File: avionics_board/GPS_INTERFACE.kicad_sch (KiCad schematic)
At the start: 2 parts, among them J6 Conn_01x05

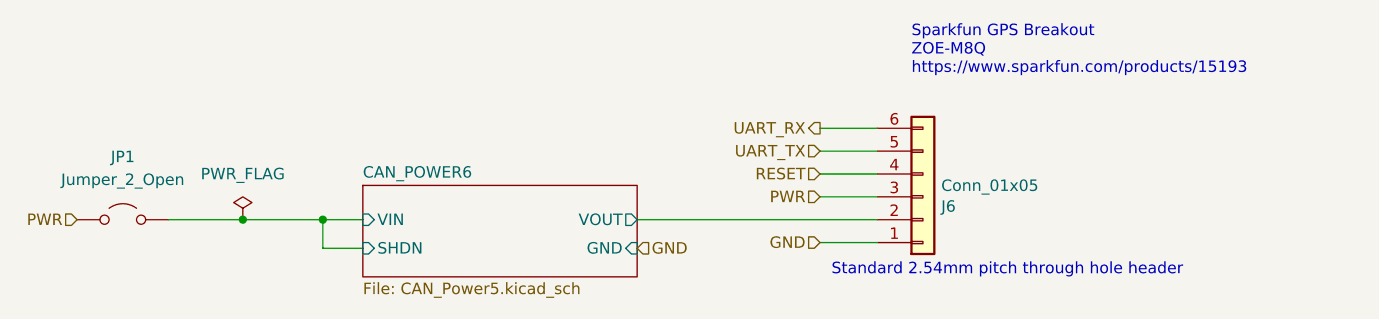
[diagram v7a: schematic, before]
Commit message: refactor AVI into nicer hierarchical components
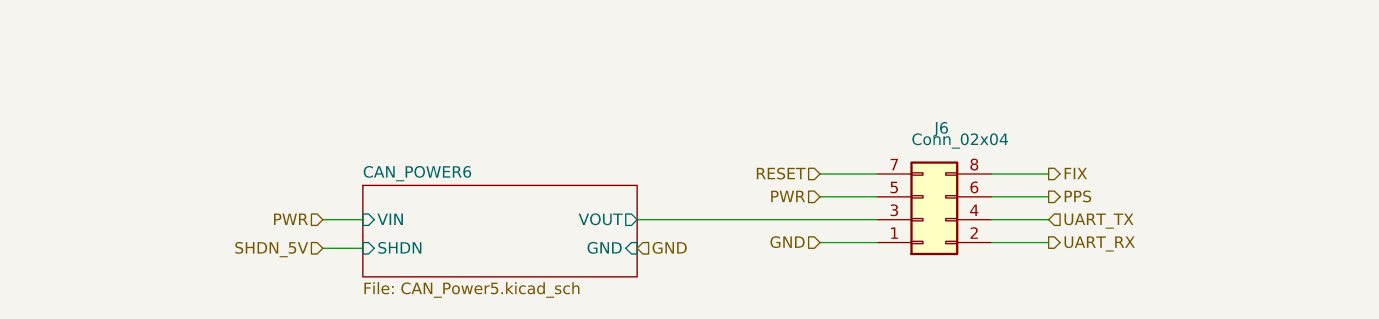
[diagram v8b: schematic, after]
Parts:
- removed J6: Conn_01x05, Connector_PinHeader_2.54mm:PinHeader_1x06_P2.54mm_Vertical, symbol Connector_Generic:Conn_01x06
- removed JP1: Jumper_2_Open, Connector_PinHeader_2.54mm:PinHeader_1x02_P2.54mm_Vertical, symbol Jumper:Jumper_2_Open
- added J6: Conn_02x04, Connector_PinHeader_2.54mm:PinHeader_2x04_P2.54mm_Vertical, symbol Connector_Generic:Conn_02x04_Odd_Even
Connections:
- net CAN_POWER6/VOUT: now also J6.3 (Pin_3)
- net GND: now also J6.1 (Pin_1)
- net PWR: now also J6.5 (Pin_5)
- net RESET: now also J6.7 (Pin_7)
- net UART_RX: now also J6.2 (Pin_2)
- net UART_TX: now also J6.4 (Pin_4)
- new net FIX: J6.8 (Pin_8)
- new net PPS: J6.6 (Pin_6)
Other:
- note removed: "Sparkfun GPS Breakout ZOE-M8Q https://www.sparkfun.com/products/15193"
- note removed: "Standard 2.54mm pitch through hole header"
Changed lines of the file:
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@@
 		(date "2020-05-12")
 	)
-	(junction
-		(at 103.505 105.41)
-		(diameter 0)
-		(color 0 0 0 0)
-	)
-	(junction
-		(at 94.615 105.41)
-		(diameter 0)
-		(color 0 0 0 0)
-	)
 	(wire
 		(pts
@@
 	(wire
 		(pts
+			(xy 165.1 100.33) (xy 158.75 100.33)
+		)
+		(stroke
+			(width 0)
+			(type default)
+		)
+	)
+	(wire
+		(pts
 			(xy 103.505 105.41) (xy 107.95 105.41)
 		)
@@
 	(wire
 		(pts
-			(xy 165.1 100.33) (xy 158.75 100.33)
-		)
-		(stroke
-			(width 0)
-			(type default)
-		)
-	)
-	(wire
-		(pts
-			(xy 86.36 105.41) (xy 94.615 105.41)
-		)
-		(stroke
-			(width 0)
-			(type default)
-		)
-	)
-	(wire
-		(pts
 			(xy 138.43 105.41) (xy 165.1 105.41)
 		)
@@
 	(wire
 		(pts
-			(xy 94.615 105.41) (xy 103.505 105.41)
-		)
-		(stroke
-			(width 0)
-			(type default)
-		)
-	)
-	(wire
-		(pts
-			(xy 165.1 97.79) (xy 158.75 97.79)
-		)
-		(stroke
-			(width 0)
-			(type default)
-		)
-	)
-	(wire
-		(pts
-			(xy 158.75 95.25) (xy 165.1 95.25)
-		)
-		(stroke
-			(width 0)
-			(type default)
-		)
-	)
-	(wire
-		(pts
-			(xy 103.505 108.585) (xy 103.505 105.41)
+			(xy 184.15 102.87) (xy 177.8 102.87)
+		)
+		(stroke
+			(width 0)
+			(type default)
+		)
+	)
+	(wire
+		(pts
+			(xy 184.15 100.33) (xy 177.8 100.33)
+		)
+		(stroke
+			(width 0)
+			(type default)
+		)
+	)
+	(wire
+		(pts
+			(xy 177.8 107.95) (xy 184.15 107.95)
+		)
+		(stroke
+			(width 0)
+			(type default)
+		)
+	)
+	(wire
+		(pts
+			(xy 184.15 105.41) (xy 177.8 105.41)
 		)
 		(stroke
@@
 		)
 	)
-	(text "Sparkfun GPS Breakout \nZOE-M8Q\nhttps://www.sparkfun.com/products/15193\n\n"
-		(exclude_from_sim no)
-		(at 168.91 91.44 0)
-		(effects
-			(font
-				(size 1.27 1.27)
-			)
-			(justify left bottom)
-		)
-	)
-	(text "Standard 2.54mm pitch through hole header"
-		(exclude_from_sim no)
-		(at 160.02 111.76 0)
-		(effects
-			(font
-				(size 1.27 1.27)
-			)
-			(justify left bottom)
-		)
-	)
 	(hierarchical_label "RESET"
 		(shape input)
@@
 		)
 	)
+	(hierarchical_label "FIX"
+		(shape output)
+		(at 184.15 100.33 0)
+		(fields_autoplaced yes)
+		(effects
+			(font
+				(size 1.27 1.27)
+			)
+			(justify left)
+		)
+	)
 	(hierarchical_label "PWR"
 		(shape input)
-		(at 76.2 105.41 180)
-		(fields_autoplaced yes)
-		(effects
-			(font
-				(size 1.27 1.27)
-			)
-			(justify right)
+		(at 103.505 105.41 180)
+		(fields_autoplaced yes)
+		(effects
+			(font
+				(size 1.27 1.27)
+			)
+			(justify right)
+		)
+	)
+	(hierarchical_label "SHDN_5V"
+		(shape input)
+		(at 103.505 108.585 180)
+		(fields_autoplaced yes)
+		(effects
+			(font
+				(size 1.27 1.27)
+			)
+			(justify right)
+		)
+	)
+	(hierarchical_label "PPS"
+		(shape output)
+		(at 184.15 102.87 0)
+		(fields_autoplaced yes)
+		(effects
+			(font
+				(size 1.27 1.27)
+			)
+			(justify left)
 		)
 	)
@@
 	(hierarchical_label "UART_TX"
 		(shape input)
-		(at 158.75 97.79 180)
-		(fields_autoplaced yes)
-		(effects
-			(font
-				(size 1.27 1.27)
-			)
-			(justify right)
+		(at 184.15 105.41 0)
+		(fields_autoplaced yes)
+		(effects
+			(font
+				(size 1.27 1.27)
+			)
+			(justify left)
 		)
 	)
 	(hierarchical_label "UART_RX"
 		(shape output)
-		(at 158.75 95.25 180)
-		(fields_autoplaced yes)
-		(effects
-			(font
-				(size 1.27 1.27)
-			)
-			(justify right)
+		(at 184.15 107.95 0)
+		(fields_autoplaced yes)
+		(effects
+			(font
+				(size 1.27 1.27)
+			)
+			(justify left)
 		)
 	)
 	(symbol
-		(lib_id "Jumper:Jumper_2_Open")
-		(at 81.28 105.41 0)
-		(unit 1)
-		(exclude_from_sim yes)
-		(in_bom yes)
-		(on_board yes)
-		(dnp no)
-		(fields_autoplaced yes)
-		(property "Reference" "JP1"
-			(at 81.28 98.425 0)
-			(effects
-				(font
-					(size 1.27 1.27)
-				)
-			)
-		)
-		(property "Value" "Jumper_2_Open"
-			(at 81.28 100.965 0)
-			(effects
-				(font
-					(size 1.27 1.27)
-				)
-			)
-		)
-		(property "Footprint" "Connector_PinHeader_2.54mm:PinHeader_1x02_P2.54mm_Vertical"
-			(at 81.28 105.41 0)
-			(effects
-				(font
-					(size 1.27 1.27)
-				)
-				(hide yes)
-			)
-		)
-		(property "Datasheet" "~"
-			(at 81.28 105.41 0)
-			(effects
-				(font
-					(size 1.27 1.27)
-				)
-				(hide yes)
-			)
-		)
-		(property "Description" "Jumper, 2-pole, open"
-			(at 81.28 105.41 0)
-			(effects
-				(font
-					(size 1.27 1.27)
-				)
-				(hide yes)
-			)
-		)
-		(pin "2"
-		)
-		(pin "1"
-		)
-		(instances
-			(project ""
-				(path "/f6cc00ab-17f1-4973-862f-7ac95fe70668/00000000-0000-0000-0000-00005ea31c93/00000000-0000-0000-0000-00005eab1057"
-					(reference "JP1")
-					(unit 1)
-				)
-			)
-		)
-	)
-	(symbol
-		(lib_id "power:PWR_FLAG")
-		(at 94.615 105.41 0)
-		(unit 1)
-		(exclude_from_sim no)
-		(in_bom yes)
-		(on_board yes)
-		(dnp no)
-		(fields_autoplaced yes)
-		(property "Reference" "#FLG04"
-			(at 94.615 103.505 0)
-			(effects
-				(font
-					(size 1.27 1.27)
-				)
-				(hide yes)
-			)
-		)
-		(property "Value" "PWR_FLAG"
-			(at 94.615 100.33 0)
-			(effects
-				(font
-					(size 1.27 1.27)
-				)
-			)
-		)
-		(property "Footprint" ""
-			(at 94.615 105.41 0)
-			(effects
-				(font
-					(size 1.27 1.27)
-				)
-				(hide yes)
-			)
-		)
-		(property "Datasheet" "~"
-			(at 94.615 105.41 0)
-			(effects
-				(font
-					(size 1.27 1.27)
-				)
-				(hide yes)
-			)
-		)
-		(property "Description" "Special symbol for telling ERC where power comes from"
-			(at 94.615 105.41 0)
-			(effects
-				(font
-					(size 1.27 1.27)
-				)
-				(hide yes)
-			)
-		)
-		(pin "1"
-		)
-		(instances
-			(project ""
-				(path "/f6cc00ab-17f1-4973-862f-7ac95fe70668/00000000-0000-0000-0000-00005ea31c93/00000000-0000-0000-0000-00005eab1057"
-					(reference "#FLG04")
-					(unit 1)
-				)
-			)
-		)
-	)
-	(symbol
-		(lib_id "Connector_Generic:Conn_01x06")
-		(at 170.18 102.87 0)
+		(lib_id "Connector_Generic:Conn_02x04_Odd_Even")
+		(at 170.18 105.41 0)
 		(mirror x)
 		(unit 1)
@@
 		(dnp no)
 		(property "Reference" "J6"
-			(at 172.212 103.9368 0)
+			(at 171.45 95.25 0)
 			(effects
 				(font
@@
 			)
 		)
-		(property "Value" "Conn_01x05"
-			(at 172.212 101.6254 0)
+		(property "Value" "Conn_02x04"
+			(at 168.91 96.52 0)
 			(effects
 				(font
@@
 			)
 		)
-		(property "Footprint" "Connector_PinHeader_2.54mm:PinHeader_1x06_P2.54mm_Vertical"
-			(at 170.18 102.87 0)
+		(property "Footprint" "Connector_PinHeader_2.54mm:PinHeader_2x04_P2.54mm_Vertical"
+			(at 170.18 105.41 0)
 			(effects
 				(font
@@
 		)
 		(property "Datasheet" "~"
-			(at 170.18 102.87 0)
-			(effects
-				(font
-					(size 1.27 1.27)
-				)
-				(hide yes)
-			)
-		)
-		(property "Description" "Generic connector, single row, 01x06, script generated (kicad-library-utils/schlib/autogen/connector/)"
-			(at 170.18 102.87 0)
+			(at 170.18 105.41 0)
+			(effects
+				(font
+					(size 1.27 1.27)
+				)
+				(hide yes)
+			)
+		)
+		(property "Description" "Generic connector, double row, 02x04, odd/even pin numbering scheme (row 1 odd numbers, row 2 even numbers), script generated (kicad-library-utils/schlib/autogen/connector/)"
+			(at 170.18 105.41 0)
 			(effects
 				(font
@@
 		)
 		(property "Order" "https://www.digikey.com/product-detail/en/adam-tech/PH1-05-UA/2057-PH1-05-UA-ND/9830343"
-			(at 170.18 102.87 0)
+			(at 170.18 105.41 0)
 			(effects
 				(font
@@
 		)
 		(property "Alt" ""
-			(at 170.18 102.87 0)
+			(at 170.18 105.41 0)
 			(effects
 				(font
@@
 		)
 		(pin "6"
+		)
+		(pin "7"
+		)
+		(pin "8"
 		)
 		(instances
 			(project "AVIONICS_BOARD"
-				(path "/f6cc00ab-17f1-4973-862f-7ac95fe70668/00000000-0000-0000-0000-00005ea31c93/00000000-0000-0000-0000-00005eab1057"
+				(path "/f6cc00ab-17f1-4973-862f-7ac95fe70668/5de22591-2293-4710-b038-9e93720cba0f"
 					(reference "J6")
 					(unit 1)
@@
 		(instances
 			(project "AVIONICS_BOARD"
-				(path "/f6cc00ab-17f1-4973-862f-7ac95fe70668/00000000-0000-0000-0000-00005ea31c93/00000000-0000-0000-0000-00005eab1057"
+				(path "/f6cc00ab-17f1-4973-862f-7ac95fe70668/5de22591-2293-4710-b038-9e93720cba0f"
 					(page "36")
 				)
